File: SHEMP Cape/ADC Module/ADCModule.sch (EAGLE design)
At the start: 51 parts, among them U1 ADS8568_PM_64, U2 LP2950-3.3ACZ

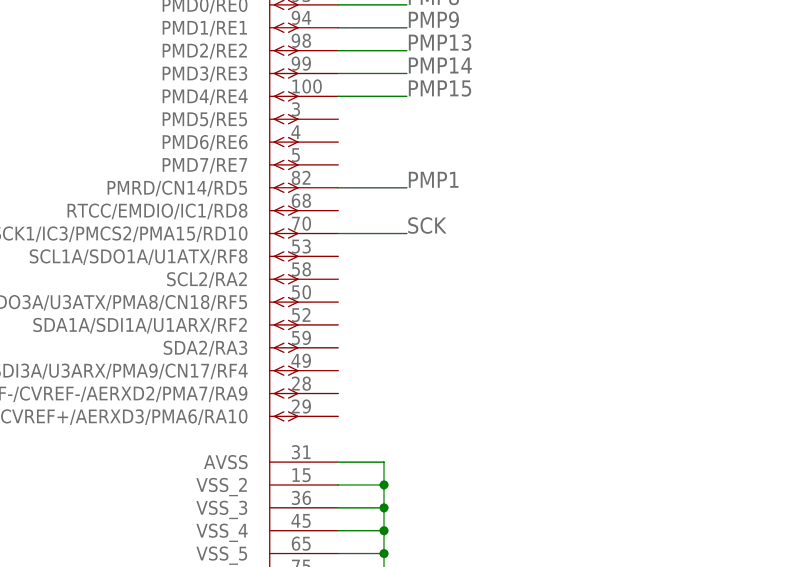
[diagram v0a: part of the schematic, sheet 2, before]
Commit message: Changed the ADC Module board for boardrouter considerations.
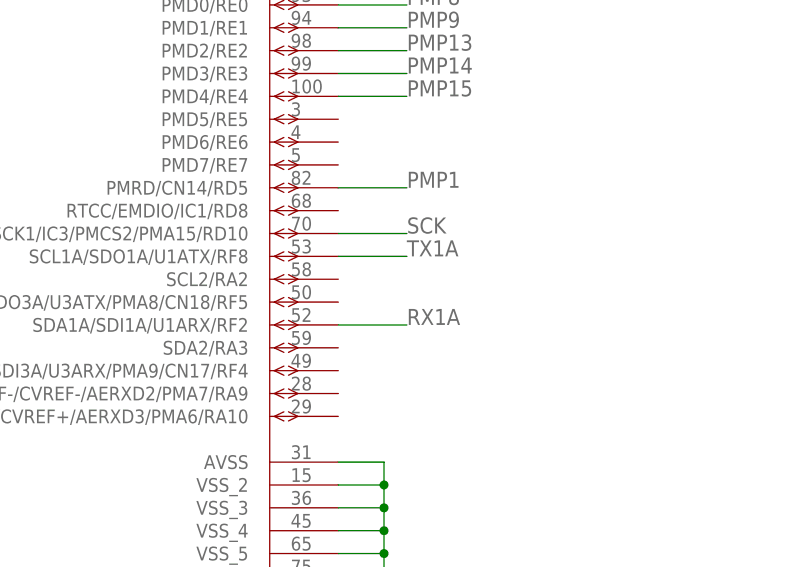
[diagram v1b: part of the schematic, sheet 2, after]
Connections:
- new net RX1A: U$1.SDA1A/SDI1A/U1ARX/RF2
- new net TX1A: U$1.SCL1A/SDO1A/U1ATX/RF8
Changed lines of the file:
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@@
 <?xml version="1.0" encoding="utf-8"?>
 <!DOCTYPE eagle SYSTEM "eagle.dtd">
-<eagle version="6.5.0">
+<eagle version="6.4">
 <drawing>
 <settings>
@@
 </segment>
 </net>
+<net name="TX1A" class="0">
+<segment>
+<pinref part="U$1" gate="A" pin="SCL1A/SDO1A/U1ATX/RF8"/>
+<wire x1="335.28" y1="88.9" x2="342.9" y2="88.9" width="0.1524" layer="91"/>
+<label x="342.9" y="88.9" size="1.778" layer="95"/>
+</segment>
+</net>
+<net name="RX1A" class="0">
+<segment>
+<pinref part="U$1" gate="A" pin="SDA1A/SDI1A/U1ARX/RF2"/>
+<wire x1="335.28" y1="81.28" x2="342.9" y2="81.28" width="0.1524" layer="91"/>
+<label x="342.9" y="81.28" size="1.778" layer="95"/>
+</segment>
+</net>

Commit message: Added new gerbers for boardrouter.
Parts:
- removed JP3: M03SCREW_LOCK, ASL:M03SCREW_LOCK
- added JP1: M03-SCREW-5MM, ASL:M03-SCREW-5MM
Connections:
- net N$1: now also JP1.3; no longer JP3.3
- net N$2: now also JP1.2; no longer JP3.2
- net N$3: now also JP1.1; no longer JP3.1
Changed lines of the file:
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@@
 <?xml version="1.0" encoding="utf-8"?>
 <!DOCTYPE eagle SYSTEM "eagle.dtd">
-<eagle version="6.4">
+<eagle version="6.5.0">
 <drawing>
 <settings>
@@
 <part name="C6" library="SensorCape" deviceset="CAP" device="0805" value="10uF"/>
 <part name="C7" library="SensorCape" deviceset="CAP" device="0805" value="10uF"/>
-<part name="JP3" library="ASL" deviceset="M03" device="SCREW_LOCK"/>
 <part name="JP4" library="ASL" deviceset="M06" device="SIP"/>
 <part name="U2" library="ASL" deviceset="LP2950" device="ACZ" technology="-3.3"/>
@@
 <part name="LED1" library="ASL" deviceset="LED" device="0805"/>
 <part name="R3" library="SensorCape" deviceset="RESISTOR" device="0805-RES"/>
+<part name="JP1" library="ASL" deviceset="M03" device="-SCREW-5MM"/>
 </parts>
 <sheets>
@@
 <instance part="C73" gate="G$1" x="347.98" y="137.16"/>
 <instance part="C74" gate="G$1" x="360.68" y="144.78" rot="R180"/>
-<instance part="JP3" gate="G$1" x="355.6" y="109.22" rot="R180"/>
 <instance part="JP4" gate="G$1" x="340.36" y="93.98" rot="R90"/>
 <instance part="JP5" gate="G$1" x="55.88" y="185.42"/>
+<instance part="JP1" gate="G$1" x="355.6" y="109.22" rot="R180"/>
 </instances>
 <busses>
@@
 <net name="N$1" class="0">
 <segment>
-<pinref part="JP3" gate="G$1" pin="3"/>
 <wire x1="347.98" y1="111.76" x2="335.28" y2="111.76" width="0.1524" layer="91"/>
 <pinref part="JP4" gate="G$1" pin="2"/>
 <wire x1="335.28" y1="111.76" x2="335.28" y2="99.06" width="0.1524" layer="91"/>
+<pinref part="JP1" gate="G$1" pin="3"/>
 </segment>
 </net>
 <net name="N$2" class="0">
 <segment>
-<pinref part="JP3" gate="G$1" pin="2"/>
 <wire x1="347.98" y1="109.22" x2="340.36" y2="109.22" width="0.1524" layer="91"/>
 <pinref part="JP4" gate="G$1" pin="4"/>
 <wire x1="340.36" y1="109.22" x2="340.36" y2="99.06" width="0.1524" layer="91"/>
+<pinref part="JP1" gate="G$1" pin="2"/>
 </segment>
 </net>
 <net name="N$3" class="0">
 <segment>
-<pinref part="JP3" gate="G$1" pin="1"/>
 <wire x1="347.98" y1="106.68" x2="345.44" y2="106.68" width="0.1524" layer="91"/>
 <pinref part="JP4" gate="G$1" pin="6"/>
 <wire x1="345.44" y1="106.68" x2="345.44" y2="99.06" width="0.1524" layer="91"/>
-</segment>
-</net>
+<pinref part="JP1" gate="G$1" pin="1"/>
+</segment>
+</net>
